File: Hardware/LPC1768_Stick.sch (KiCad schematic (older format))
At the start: 85 parts, among them CON1 BARREL_JACK, CON2 USB-MINI-B, IC1 LM1117, IC2 LM1117, P1 CONN_01X40, P2 JTAG, P3 CONN_01X40, P4 USB Operation Selection, Q1 BC856, SW1 RST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

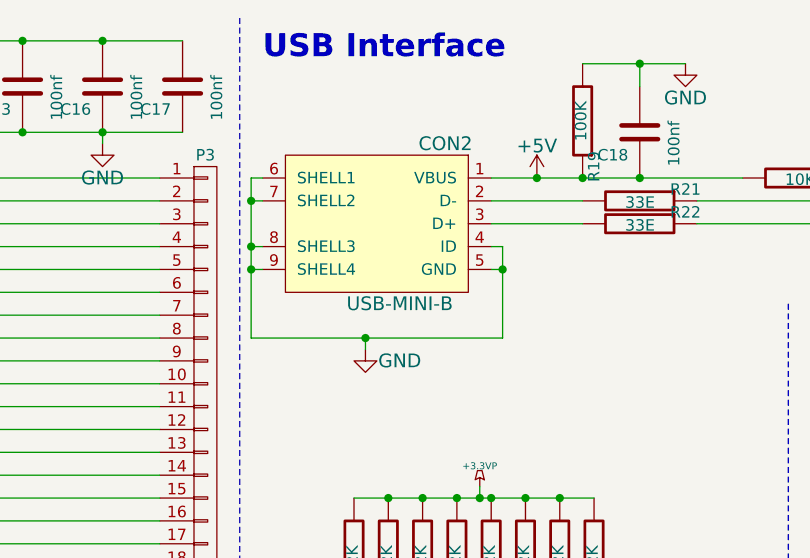
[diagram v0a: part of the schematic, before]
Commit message: Changed USB Connector
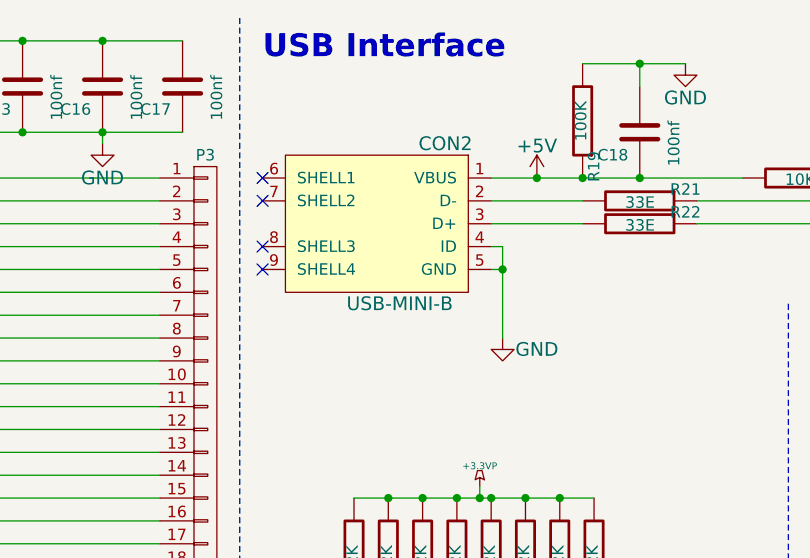
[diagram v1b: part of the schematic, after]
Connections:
- net GND: no longer CON2.6 (SHELL1), CON2.7 (SHELL2), CON2.8 (SHELL3), CON2.9 (SHELL4)
- no-connect marks 5 -> 9
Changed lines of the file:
@@
 L GND #PWR013
 U 1 1 5512B02A
-P 7250 1900
-F 0 "#PWR013" H 7250 1650 60  0001 C CNN
-F 1 "GND" H 7400 1850 60  0000 C CNN
-F 2 "" H 7250 1900 60  0000 C CNN
-F 3 "" H 7250 1900 60  0000 C CNN
-	1    7250 1900
+P 7850 1850
+F 0 "#PWR013" H 7850 1600 60  0001 C CNN
+F 1 "GND" H 8000 1800 60  0000 C CNN
+F 2 "" H 7850 1850 60  0000 C CNN
+F 3 "" H 7850 1850 60  0000 C CNN
+	1    7850 1850
 	1    0    0    -1
 $EndComp
@@
 SDA_3
 Wire Wire Line
-	6750 1150 6750 1850
-Connection ~ 6750 1250
-Connection ~ 6750 1450
-Wire Wire Line
-	6750 1850 7850 1850
-Wire Wire Line
 	7850 1850 7850 1450
-Connection ~ 6750 1550
 Connection ~ 7850 1550
-Wire Wire Line
-	7250 1850 7250 1900
-Connection ~ 7250 1850
 NoConn ~ 2950 2000
 NoConn ~ 5350 5150
@@
 	10250 6150 10450 6150
 Wire Wire Line
-	6800 1150 6750 1150
-Wire Wire Line
-	6800 1250 6750 1250
-Wire Wire Line
-	6800 1450 6750 1450
-Wire Wire Line
-	6800 1550 6750 1550
-Wire Wire Line
 	7850 1550 7800 1550
 Wire Wire Line
@@
 	1    0    0    -1
 $EndComp
+NoConn ~ 6800 1150
+NoConn ~ 6800 1250
+NoConn ~ 6800 1450
+NoConn ~ 6800 1550
 $EndSCHEMATC
